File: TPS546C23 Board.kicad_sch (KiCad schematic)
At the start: 40 parts, among them IC1 TPS546C23RVFT, J1 Conn_01x01, J2 Conn_01x01, J3 Conn_01x01, J4 Conn_01x01, J7 Conn_01x02_Pin

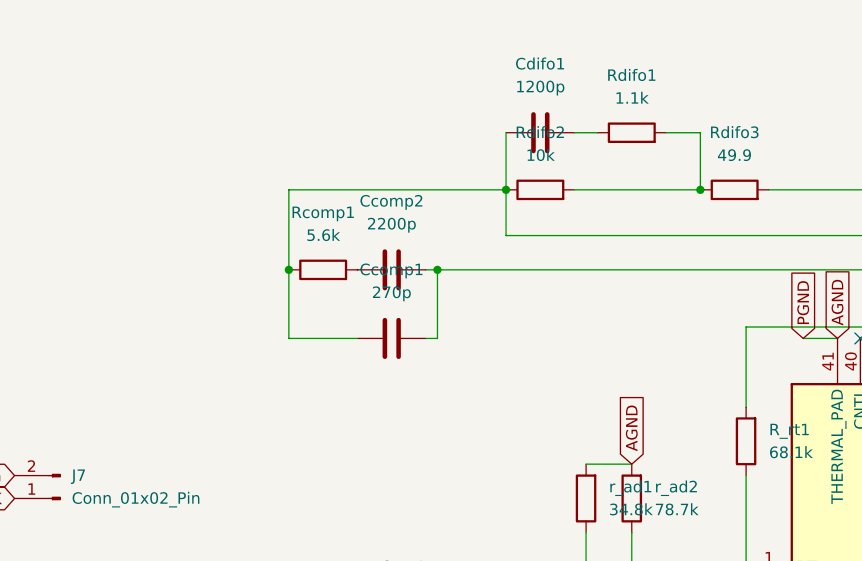
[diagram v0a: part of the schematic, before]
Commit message: added Rbias for full voltage range
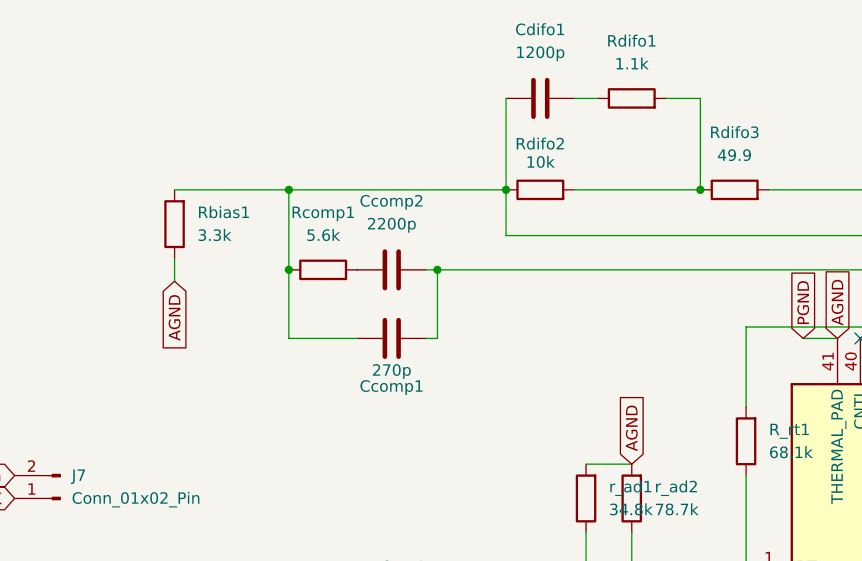
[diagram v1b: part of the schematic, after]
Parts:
- added Rbias1: 3.3k, Resistor_SMD:R_0402_1005Metric, symbol Device:R
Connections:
- net AGND: now also Rbias1.1
- net at Ccomp1.2, Cdifo1.2, IC1.36 (FB)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: now also Rbias1.2
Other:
- moved on the sheet: Cdifo1, Rdifo1
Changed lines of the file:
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@@
 	)
 	(junction
+		(at 91.44 48.26)
+		(diameter 0)
+		(color 0 0 0 0)
+	)
+	(junction
 		(at 212.09 118.11)
 		(diameter 0)
@@
 	(wire
 		(pts
-			(xy 133.35 41.91) (xy 137.16 41.91)
+			(xy 133.35 38.1) (xy 137.16 38.1)
 		)
 		(stroke
@@
 	(wire
 		(pts
-			(xy 137.16 48.26) (xy 137.16 41.91)
+			(xy 137.16 48.26) (xy 137.16 38.1)
 		)
 		(stroke
@@
 	(wire
 		(pts
+			(xy 78.74 48.26) (xy 91.44 48.26)
+		)
+		(stroke
+			(width 0)
+			(type default)
+		)
+	)
+	(wire
+		(pts
 			(xy 91.44 57.15) (xy 91.44 64.77)
 		)
@@
 	(wire
 		(pts
-			(xy 115.57 41.91) (xy 115.57 48.26)
+			(xy 115.57 38.1) (xy 115.57 48.26)
 		)
 		(stroke
@@
 	(wire
 		(pts
+			(xy 78.74 55.88) (xy 78.74 58.42)
+		)
+		(stroke
+			(width 0)
+			(type default)
+		)
+	)
+	(wire
+		(pts
 			(xy 194.31 93.98) (xy 194.31 97.79)
 		)
@@
 	(wire
 		(pts
-			(xy 123.19 41.91) (xy 125.73 41.91)
+			(xy 123.19 38.1) (xy 125.73 38.1)
 		)
 		(stroke
@@
 		)
 	)
+	(global_label "AGND"
+		(shape input)
+		(at 78.74 58.42 270)
+		(fields_autoplaced yes)
+		(effects
+			(font
+				(size 1.27 1.27)
+			)
+			(justify right)
+		)
+		(property "Intersheetrefs" "${INTERSHEET_REFS}"
+			(at 78.74 66.3643 90)
+			(hide yes)
+			(show_name no)
+			(do_not_autoplace no)
+			(effects
+				(font
+					(size 1.27 1.27)
+				)
+				(justify right)
+			)
+		)
+	)
 	(global_label "PGND"
 		(shape input)
@@
 		(in_pos_files yes)
 		(dnp no)
-		(fields_autoplaced yes)
 		(property "Reference" "Ccomp1"
-			(at 102.87 57.15 90)
+			(at 102.87 70.104 90)
 			(show_name no)
 			(do_not_autoplace no)
@@
 		)
 		(property "Value" "270p"
-			(at 102.87 59.69 90)
+			(at 102.87 68.326 90)
 			(show_name no)
 			(do_not_autoplace no)
@@
 	(symbol
 		(lib_id "Device:C")
-		(at 119.38 41.91 270)
+		(at 119.38 38.1 270)
 		(unit 1)
 		(body_style 1)
@@
 		(fields_autoplaced yes)
 		(property "Reference" "Cdifo1"
-			(at 119.38 34.29 90)
+			(at 119.38 30.48 90)
 			(show_name no)
 			(do_not_autoplace no)
@@
 		)
 		(property "Value" "1200p"
-			(at 119.38 36.83 90)
+			(at 119.38 33.02 90)
 			(show_name no)
 			(do_not_autoplace no)
@@
 		)
 		(property "Footprint" "Capacitor_SMD:C_0402_1005Metric"
-			(at 115.57 42.8752 0)
+			(at 115.57 39.0652 0)
 			(hide yes)
 			(show_name no)
@@
 		)
 		(property "Datasheet" ""
-			(at 119.38 41.91 0)
+			(at 119.38 38.1 0)
 			(hide yes)
 			(show_name no)
@@
 		)
 		(property "Description" "Unpolarized capacitor"
-			(at 119.38 41.91 0)
+			(at 119.38 38.1 0)
 			(hide yes)
 			(show_name no)
@@
 	(symbol
 		(lib_id "Device:R")
-		(at 129.54 41.91 90)
+		(at 129.54 38.1 90)
 		(unit 1)
 		(body_style 1)
@@
 		(fields_autoplaced yes)
 		(property "Reference" "Rdifo1"
-			(at 129.54 35.56 90)
+			(at 129.54 31.75 90)
 			(show_name no)
 			(do_not_autoplace no)
@@
 		)
 		(property "Value" "1.1k"
-			(at 129.54 38.1 90)
+			(at 129.54 34.29 90)
 			(show_name no)
 			(do_not_autoplace no)
@@
 		)
 		(property "Footprint" "Resistor_SMD:R_0402_1005Metric"
-			(at 129.54 43.688 90)
+			(at 129.54 39.878 90)
 			(hide yes)
 			(show_name no)
@@
 		)
 		(property "Datasheet" ""
-			(at 129.54 41.91 0)
+			(at 129.54 38.1 0)
 			(hide yes)
 			(show_name no)
@@
 		)
 		(property "Description" "Resistor"
-			(at 129.54 41.91 0)
+			(at 129.54 38.1 0)
 			(hide yes)
 			(show_name no)
@@
 		(in_pos_files yes)
 		(dnp no)
-		(fields_autoplaced yes)
 		(property "Reference" "Rdifo2"
-			(at 119.38 41.91 90)
+			(at 119.38 43.18 90)
 			(show_name no)
 			(do_not_autoplace no)
@@
 		)
 		(property "Value" "10k"
-			(at 119.38 44.45 90)
+			(at 119.38 45.212 90)
 			(show_name no)
 			(do_not_autoplace no)
@@
 					(unit 1)
 				)
+			)
+		)
+	)
+	(symbol
+		(lib_id "Device:R")
+		(at 78.74 52.07 180)
+		(unit 1)
+		(body_style 1)
+		(exclude_from_sim no)
+		(in_bom yes)
+		(on_board yes)
+		(in_pos_files yes)
+		(dnp no)
+		(fields_autoplaced yes)
+		(property "Reference" "Rbias1"
+			(at 81.28 50.7999 0)
+			(show_name no)
+			(do_not_autoplace no)
+			(effects
+				(font
+					(size 1.27 1.27)
+				)
+				(justify right)
+			)
+		)
+		(property "Value" "3.3k"
+			(at 81.28 53.3399 0)
+			(show_name no)
+			(do_not_autoplace no)
+			(effects
+				(font
+					(size 1.27 1.27)
+				)
+				(justify right)
+			)
+		)
+		(property "Footprint" "Resistor_SMD:R_0402_1005Metric"
+			(at 80.518 52.07 90)
+			(hide yes)
+			(show_name no)
+			(do_not_autoplace no)
+			(effects
+				(font
+					(size 1.27 1.27)
+				)
+			)
+		)
+		(property "Datasheet" ""
+			(at 78.74 52.07 0)
+			(hide yes)
+			(show_name no)
+			(do_not_autoplace no)
+			(effects
+				(font
+					(size 1.27 1.27)
+				)
+			)
+		)
+		(property "Description" "Resistor"
+			(at 78.74 52.07 0)
+			(hide yes)
+			(show_name no)
+			(do_not_autoplace no)
+			(effects
+				(font
+					(size 1.27 1.27)
+				)
+			)
+		)
+		(pin "2"
+		)
+		(pin "1"
+		)
+		(instances
+			(project "TPS546C23 Board"
+				(path "/960453c9-4812-426e-be09-fe8f88aa18c9"
+					(reference "Rbias1")
+					(unit 1)
+				)

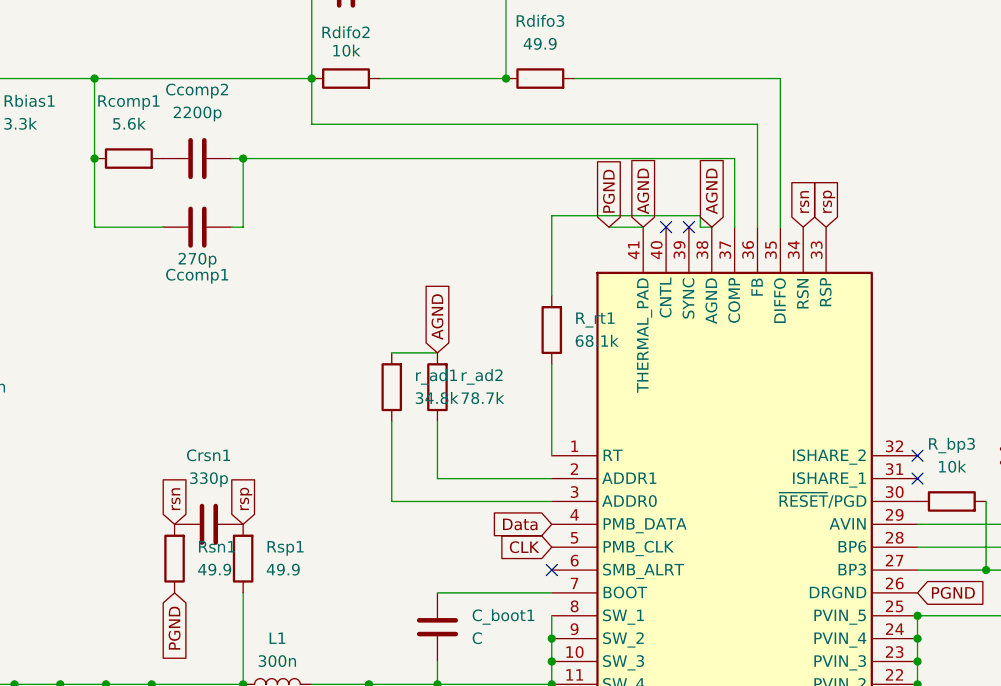
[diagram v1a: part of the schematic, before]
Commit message: added voltage divider resistor, changed to 4 layer
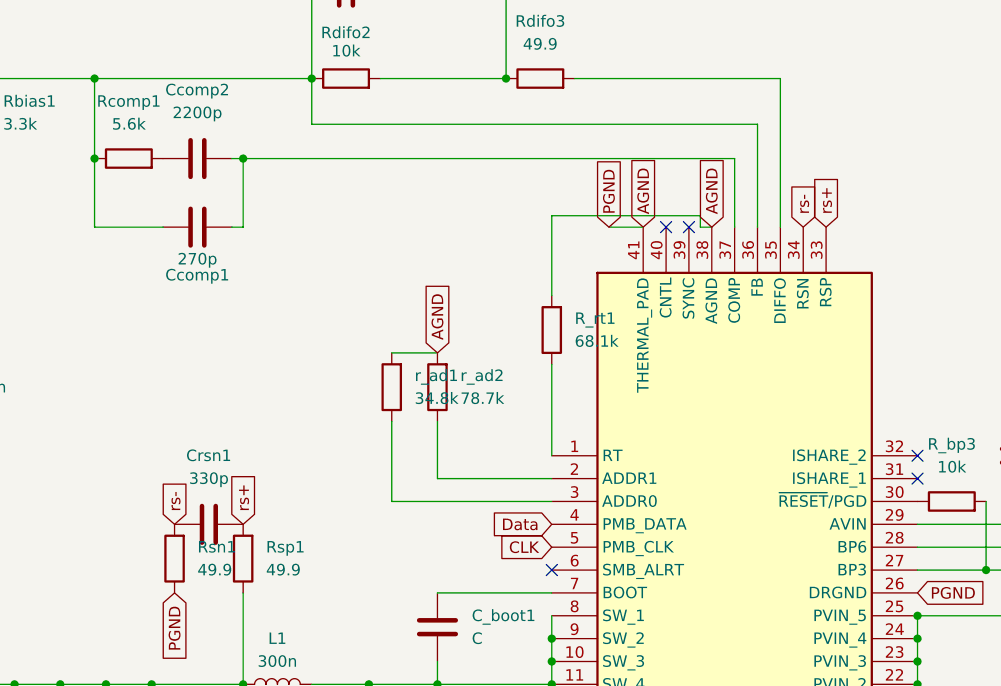
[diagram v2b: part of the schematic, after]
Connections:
- net rsn renamed rs-
- net rsp renamed rs+
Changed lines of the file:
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@@
 		)
 	)
-	(global_label "rsn"
+	(global_label "rs-"
 		(shape input)
 		(at 100.33 97.79 90)
@@
 		)
 		(property "Intersheetrefs" "${INTERSHEET_REFS}"
-			(at 100.33 91.8415 90)
+			(at 100.33 91.4181 90)
 			(hide yes)
 			(show_name no)
@@
 		)
 	)
-	(global_label "rsp"
+	(global_label "rs+"
 		(shape input)
 		(at 107.95 97.79 90)
@@
 		)
 		(property "Intersheetrefs" "${INTERSHEET_REFS}"
-			(at 107.95 91.8415 90)
-			(hide yes)
-			(show_name no)
-			(do_not_autoplace no)
-			(effects
-				(font
-					(size 1.27 1.27)
-				)
-				(justify left)
-			)
-		)
-	)
-	(global_label "rsn"
+			(at 107.95 91.4181 90)
+			(hide yes)
+			(show_name no)
+			(do_not_autoplace no)
+			(effects
+				(font
+					(size 1.27 1.27)
+				)
+				(justify left)
+			)
+		)
+	)
+	(global_label "rs-"
 		(shape input)
 		(at 170.18 64.77 90)
@@
 		)
 	)
-	(global_label "rsp"
+	(global_label "rs+"
 		(shape input)
 		(at 172.72 64.77 90)
